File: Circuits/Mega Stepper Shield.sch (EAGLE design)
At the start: 14 parts

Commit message: Update CAD
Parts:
- removed POWER, STBY, STOP-1, STOP-2, STOP-3: (no value), con-wago-500:W237-102
- added EXTERNAL: (no value), con-wago-508:W237-09P
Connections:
- net 12V10A: now also EXTERNAL-1.KL; no longer POWER-1.KL
- net GND: now also EXTERNAL-3.KL, EXTERNAL-6.KL; no longer STBY-1.KL, STOP-1-2.KL, STOP-2-2.KL, STOP-3-2.KL
- net N$1: now also EXTERNAL-9.KL; no longer STOP-3-1.KL
- net N$11: now also EXTERNAL-2.KL; no longer POWER-2.KL
- net N$12: now also EXTERNAL-8.KL; no longer STOP-2-1.KL
- net N$13: now also EXTERNAL-4.KL; no longer STBY-2.KL
- net N$14: now also EXTERNAL-7.KL; no longer STOP-1-1.KL
- net N$2: now also EXTERNAL-5.KL

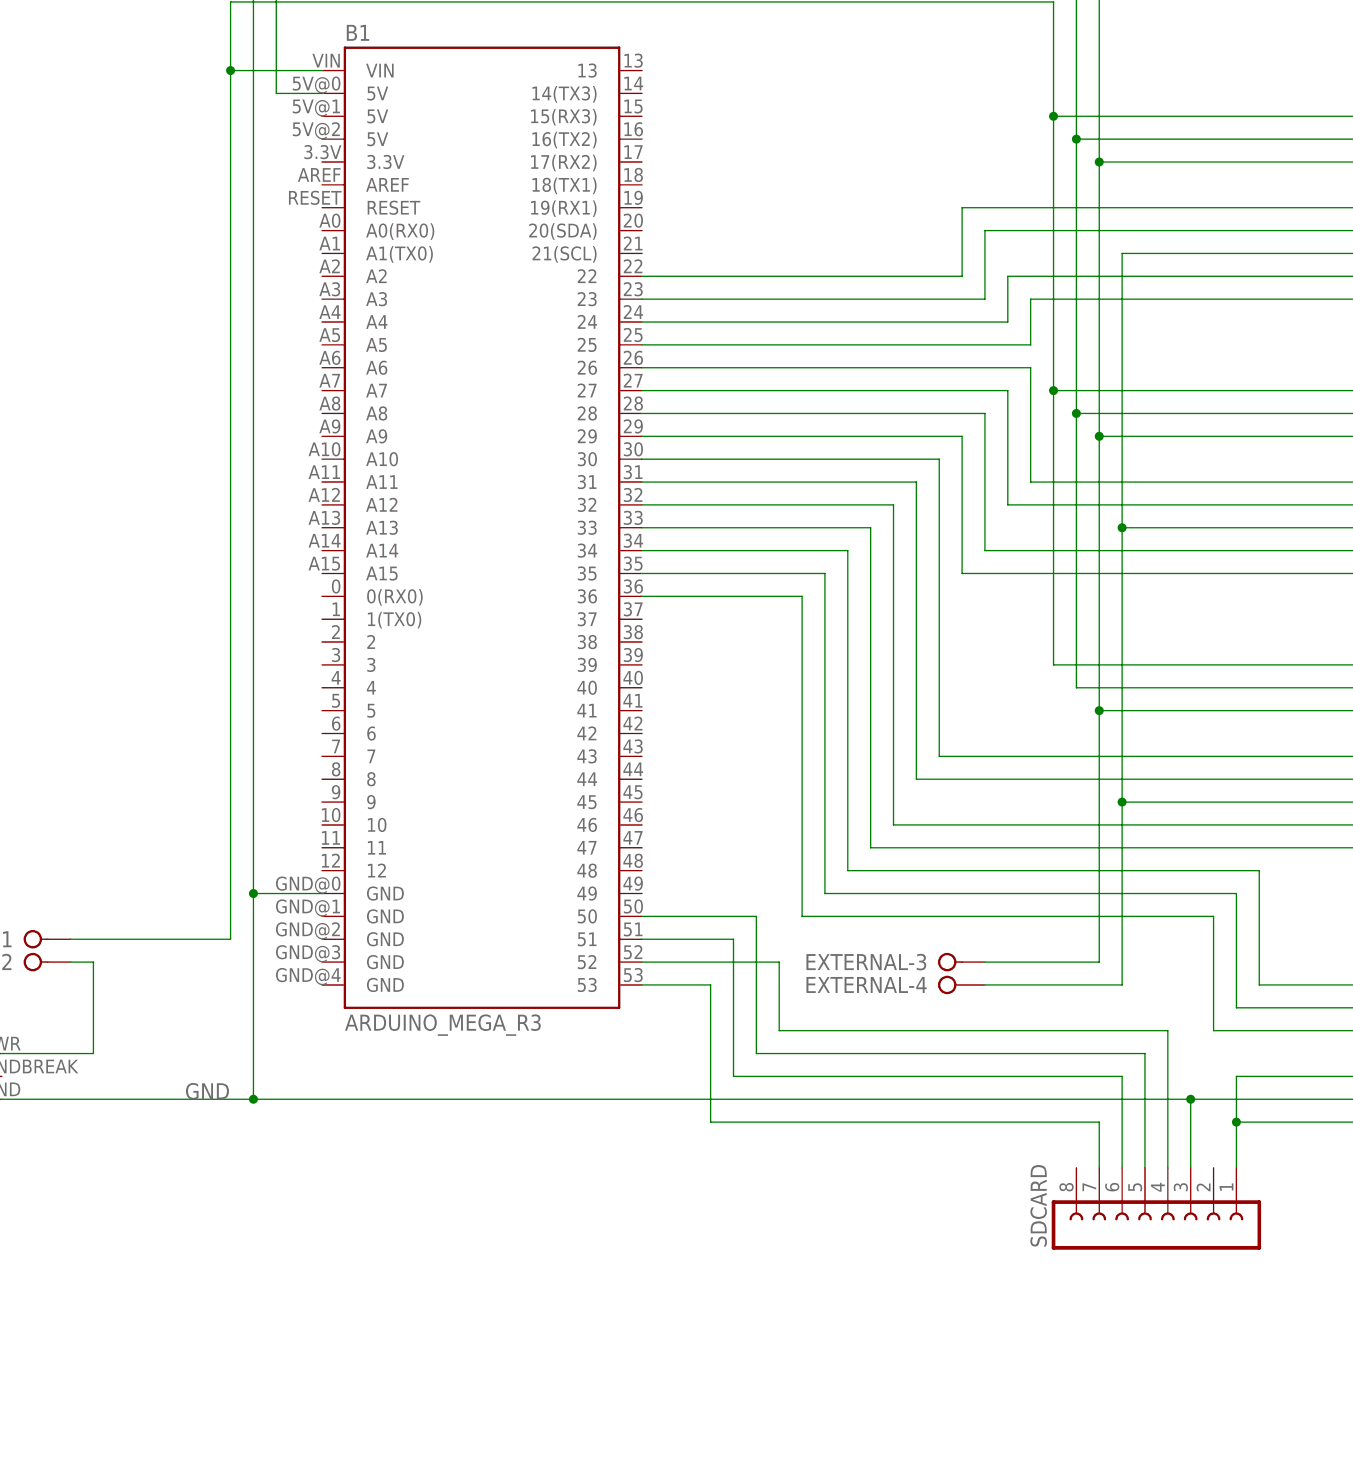
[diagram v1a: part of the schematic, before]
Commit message: Update schematic and prototype schematic
Added RF module to schematic, created a prototype sub board for multiple stepper control
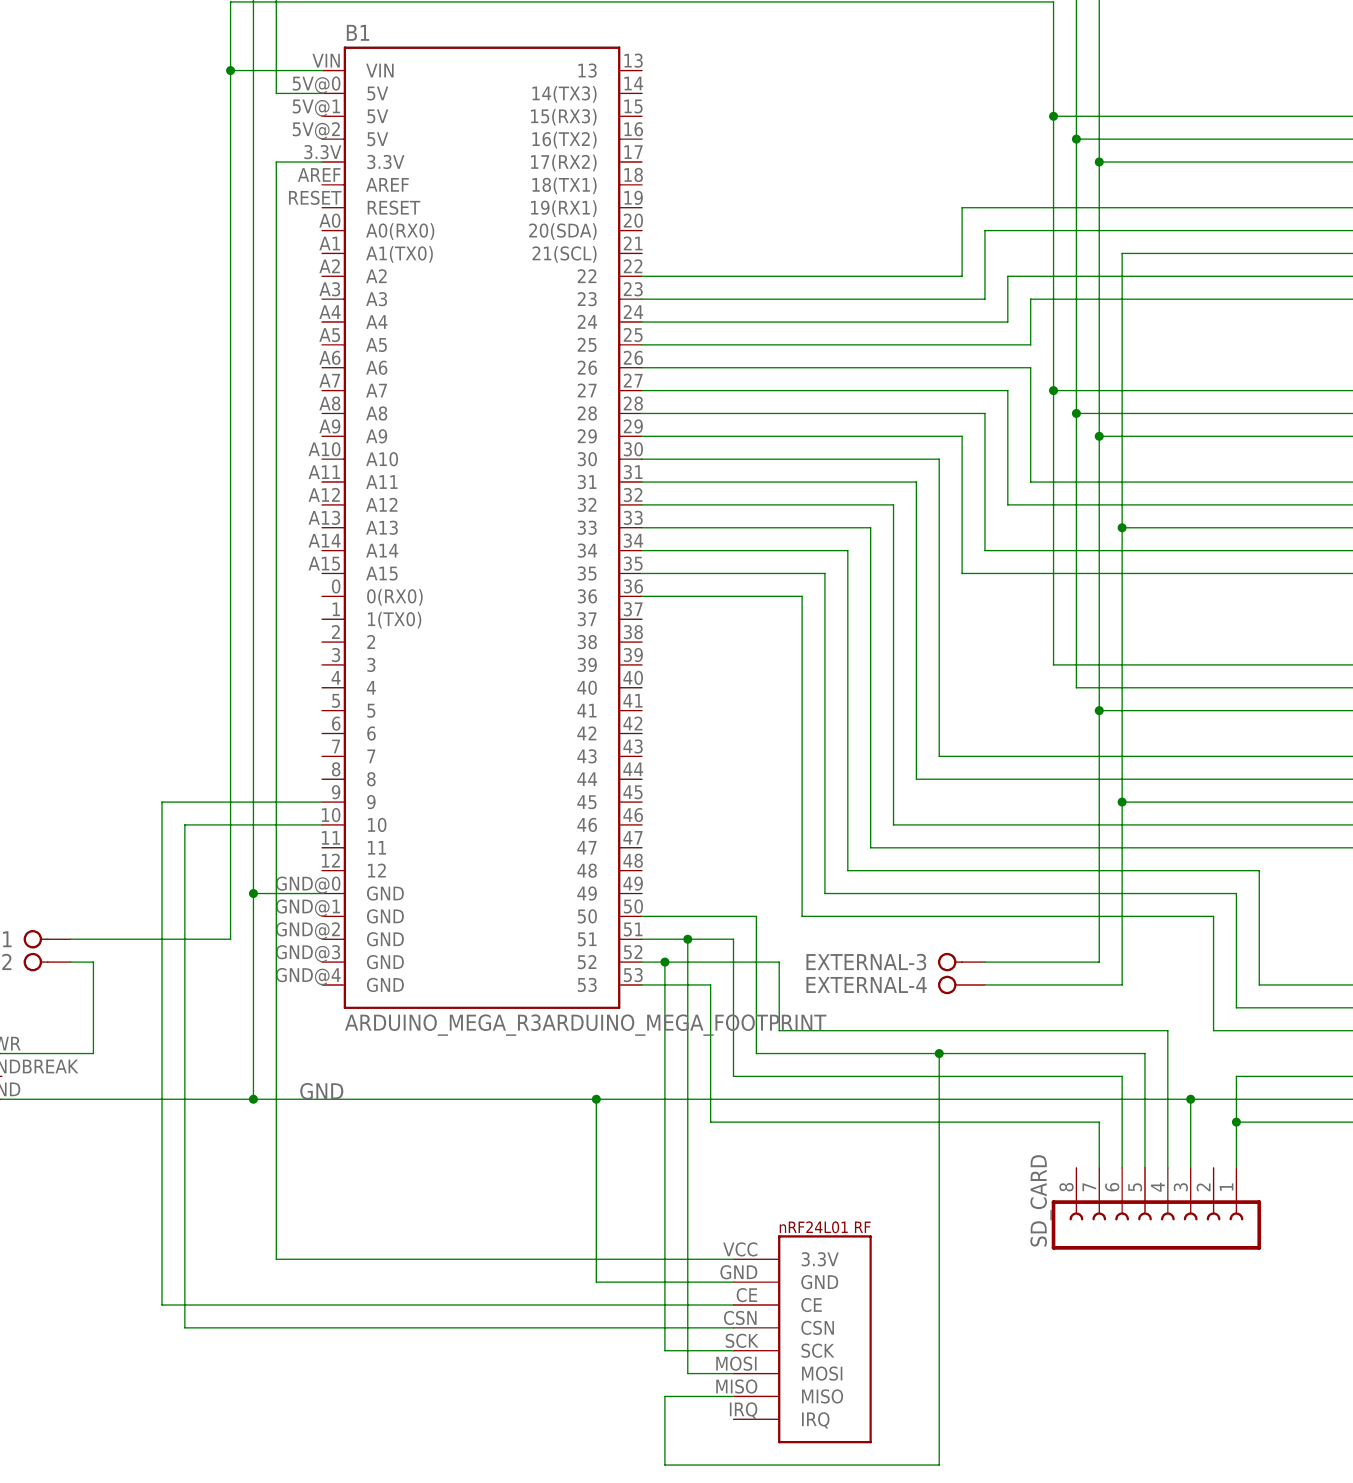
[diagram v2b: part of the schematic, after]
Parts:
- added U$1: NRF24L01_RF_MODULE, SparkFun-Boards-Expanded:NRF24L01_RF_MODULE
- B1: value ARDUINO_MEGA_R3 -> ARDUINO_MEGA_R3ARDUINO_MEGA_FOOTPRINT; device SparkFun-Boards-Expanded:ARDUINO_MEGA_R3 -> SparkFun-Boards-Expanded:ARDUINO_MEGA_R3ARDUINO_MEGA_FOOTPRINT
- renumbered SDCARD to SD_CARD
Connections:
- new net N$32: B1.3.3V, U$1.3.3V
- new net N$34: B1.9, U$1.CE
- new net N$35: B1.10, U$1.CSN
- net GND: now also U$1.GND
- net N$28: now also U$1.SCK
- net N$29: now also U$1.MISO
- net N$30: now also U$1.MOSI
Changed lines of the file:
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@@
 </classes>
 <parts>
-<part name="B1" library="SparkFun-Boards-Expanded" deviceset="ARDUINO_MEGA_R3" device=""/>
+<part name="B1" library="SparkFun-Boards-Expanded" deviceset="ARDUINO_MEGA_R3" device="ARDUINO_MEGA_FOOTPRINT" value="ARDUINO_MEGA_R3ARDUINO_MEGA_FOOTPRINT"/>
 <part name="STEPPER-1-CON" library="SparkFun-Boards-Expanded" deviceset="TB6612-BREAKOUT-MOTOR-CONTROLLER" device=""/>
 <part name="STEPPER-2-CON" library="SparkFun-Boards-Expanded" deviceset="TB6612-BREAKOUT-MOTOR-CONTROLLER" device=""/>
@@
 <part name="STEPPER-3" library="pinhead" library_urn="urn:adsk.eagle:library:325" deviceset="PINHD-1X4" device="" package3d_urn="urn:adsk.eagle:package:22407/2"/>
 <part name="CN1" library="adafruit" library_urn="urn:adsk.eagle:library:420" deviceset="DCBARREL" device="PTH" package3d_urn="urn:adsk.eagle:package:6240729/1"/>
-<part name="SDCARD" library="con-lsta" library_urn="urn:adsk.eagle:library:161" deviceset="FE08-1" device="" package3d_urn="urn:adsk.eagle:package:8194/1"/>
+<part name="SD_CARD" library="con-lsta" library_urn="urn:adsk.eagle:library:161" deviceset="FE08-1" device="" package3d_urn="urn:adsk.eagle:package:8194/1"/>
 <part name="EXTERNAL" library="con-wago-508" library_urn="urn:adsk.eagle:library:196" deviceset="W237-09P" device="" package3d_urn="urn:adsk.eagle:package:10748/1"/>
+<part name="U$1" library="SparkFun-Boards-Expanded" deviceset="NRF24L01_RF_MODULE" device=""/>
 </parts>
 <sheets>
@@
 <attribute name="VALUE" x="-76.2" y="-66.04" size="1.27" layer="96"/>
 </instance>
-<instance part="SDCARD" gate="G$1" x="60.96" y="-78.74" smashed="yes" rot="R90">
+<instance part="SD_CARD" gate="G$1" x="60.96" y="-78.74" smashed="yes" rot="R90">
 <attribute name="VALUE" x="73.66" y="-80.01" size="1.778" layer="96" rot="R90"/>
 <attribute name="NAME" x="47.498" y="-80.01" size="1.778" layer="95" rot="R90"/>
@@
 <attribute name="NAME" x="135.89" y="-34.671" size="1.778" layer="95" rot="R180"/>
 </instance>
+<instance part="U$1" gate="G$1" x="25.4" y="-81.28" smashed="yes"/>
 </instances>
 <busses>
@@
 <junction x="86.36" y="38.1"/>
 <junction x="86.36" y="-38.1"/>
-<pinref part="SDCARD" gate="G$1" pin="1"/>
+<pinref part="SD_CARD" gate="G$1" pin="1"/>
 <wire x1="68.58" y1="-71.12" x2="68.58" y2="-66.04" width="0.1524" layer="91"/>
 <wire x1="68.58" y1="-66.04" x2="68.58" y2="-60.96" width="0.1524" layer="91"/>
@@
 <wire x1="-40.64" y1="-63.5" x2="-40.64" y2="-40.64" width="0.1524" layer="91"/>
 <junction x="-40.64" y="-40.64"/>
-<label x="-48.26" y="-63.5" size="1.778" layer="95"/>
-<wire x1="-40.64" y1="-63.5" x2="63.5" y2="-63.5" width="0.1524" layer="91"/>
+<label x="-35.56" y="-63.5" size="1.778" layer="95"/>
 <junction x="-40.64" y="-63.5"/>
-<pinref part="SDCARD" gate="G$1" pin="3"/>
+<pinref part="SD_CARD" gate="G$1" pin="3"/>
+<wire x1="-40.64" y1="-63.5" x2="-2.54" y2="-63.5" width="0.1524" layer="91"/>
+<wire x1="-2.54" y1="-63.5" x2="63.5" y2="-63.5" width="0.1524" layer="91"/>
 <wire x1="63.5" y1="-71.12" x2="63.5" y2="-63.5" width="0.1524" layer="91"/>
 <pinref part="EXTERNAL" gate="-6" pin="KL"/>
@@
 <pinref part="EXTERNAL" gate="-3" pin="KL"/>
 <wire x1="40.64" y1="-48.26" x2="53.34" y2="-48.26" width="0.1524" layer="91"/>
+<pinref part="U$1" gate="G$1" pin="GND"/>
+<wire x1="12.7" y1="-83.82" x2="-2.54" y2="-83.82" width="0.1524" layer="91"/>
+<wire x1="-2.54" y1="-83.82" x2="-2.54" y2="-63.5" width="0.1524" layer="91"/>
+<junction x="-2.54" y="-63.5"/>
 </segment>
 </net>
@@
 <net name="N$28" class="0">
 <segment>
-<pinref part="SDCARD" gate="G$1" pin="4"/>
+<pinref part="SD_CARD" gate="G$1" pin="4"/>
 <wire x1="60.96" y1="-71.12" x2="60.96" y2="-55.88" width="0.1524" layer="91"/>
 <wire x1="60.96" y1="-55.88" x2="17.78" y2="-55.88" width="0.1524" layer="91"/>
 <pinref part="B1" gate="G$1" pin="52"/>
 <wire x1="17.78" y1="-55.88" x2="17.78" y2="-48.26" width="0.1524" layer="91"/>
-<wire x1="17.78" y1="-48.26" x2="2.54" y2="-48.26" width="0.1524" layer="91"/>
+<wire x1="17.78" y1="-48.26" x2="5.08" y2="-48.26" width="0.1524" layer="91"/>
+<pinref part="U$1" gate="G$1" pin="SCK"/>
+<wire x1="5.08" y1="-48.26" x2="2.54" y2="-48.26" width="0.1524" layer="91"/>
+<wire x1="5.08" y1="-48.26" x2="5.08" y2="-91.44" width="0.1524" layer="91"/>
+<wire x1="5.08" y1="-91.44" x2="12.7" y2="-91.44" width="0.1524" layer="91"/>
+<junction x="5.08" y="-48.26"/>
 </segment>
 </net>
@@
 <wire x1="2.54" y1="-43.18" x2="15.24" y2="-43.18" width="0.1524" layer="91"/>
 <wire x1="15.24" y1="-43.18" x2="15.24" y2="-58.42" width="0.1524" layer="91"/>
-<pinref part="SDCARD" gate="G$1" pin="5"/>
-<wire x1="15.24" y1="-58.42" x2="58.42" y2="-58.42" width="0.1524" layer="91"/>
+<pinref part="SD_CARD" gate="G$1" pin="5"/>
+<wire x1="15.24" y1="-58.42" x2="35.56" y2="-58.42" width="0.1524" layer="91"/>
+<wire x1="35.56" y1="-58.42" x2="58.42" y2="-58.42" width="0.1524" layer="91"/>
 <wire x1="58.42" y1="-58.42" x2="58.42" y2="-71.12" width="0.1524" layer="91"/>
+<pinref part="U$1" gate="G$1" pin="MISO"/>
+<wire x1="12.7" y1="-96.52" x2="5.08" y2="-96.52" width="0.1524" layer="91"/>
+<wire x1="5.08" y1="-96.52" x2="5.08" y2="-104.14" width="0.1524" layer="91"/>
+<wire x1="5.08" y1="-104.14" x2="35.56" y2="-104.14" width="0.1524" layer="91"/>
+<wire x1="35.56" y1="-104.14" x2="35.56" y2="-58.42" width="0.1524" layer="91"/>
+<junction x="35.56" y="-58.42"/>
 </segment>
 </net>
 <net name="N$30" class="0">
 <segment>
-<pinref part="SDCARD" gate="G$1" pin="6"/>
+<pinref part="SD_CARD" gate="G$1" pin="6"/>
 <wire x1="55.88" y1="-71.12" x2="55.88" y2="-60.96" width="0.1524" layer="91"/>
 <wire x1="55.88" y1="-60.96" x2="12.7" y2="-60.96" width="0.1524" layer="91"/>
 <pinref part="B1" gate="G$1" pin="51"/>
 <wire x1="12.7" y1="-60.96" x2="12.7" y2="-45.72" width="0.1524" layer="91"/>
-<wire x1="12.7" y1="-45.72" x2="2.54" y2="-45.72" width="0.1524" layer="91"/>
+<wire x1="12.7" y1="-45.72" x2="7.62" y2="-45.72" width="0.1524" layer="91"/>
+<pinref part="U$1" gate="G$1" pin="MOSI"/>
+<wire x1="7.62" y1="-45.72" x2="2.54" y2="-45.72" width="0.1524" layer="91"/>
+<wire x1="12.7" y1="-93.98" x2="7.62" y2="-93.98" width="0.1524" layer="91"/>
+<wire x1="7.62" y1="-93.98" x2="7.62" y2="-45.72" width="0.1524" layer="91"/>
+<junction x="7.62" y="-45.72"/>
 </segment>
 </net>
@@
 <wire x1="2.54" y1="-50.8" x2="10.16" y2="-50.8" width="0.1524" layer="91"/>
 <wire x1="10.16" y1="-50.8" x2="10.16" y2="-66.04" width="0.1524" layer="91"/>
-<pinref part="SDCARD" gate="G$1" pin="7"/>
+<pinref part="SD_CARD" gate="G$1" pin="7"/>
 <wire x1="10.16" y1="-66.04" x2="53.34" y2="-66.04" width="0.1524" layer="91"/>
 <wire x1="53.34" y1="-66.04" x2="53.34" y2="-71.12" width="0.1524" layer="91"/>
 </segment>
 </net>
+<net name="N$32" class="0">
+<segment>
+<pinref part="B1" gate="G$1" pin="3.3V"/>
+<wire x1="-33.02" y1="40.64" x2="-38.1" y2="40.64" width="0.1524" layer="91"/>
+<wire x1="-38.1" y1="40.64" x2="-38.1" y2="-81.28" width="0.1524" layer="91"/>
+<pinref part="U$1" gate="G$1" pin="3.3V"/>
+<wire x1="-38.1" y1="-81.28" x2="12.7" y2="-81.28" width="0.1524" layer="91"/>
+</segment>
+</net>
+<net name="N$34" class="0">
+<segment>
+<pinref part="B1" gate="G$1" pin="9"/>
+<wire x1="-33.02" y1="-30.48" x2="-50.8" y2="-30.48" width="0.1524" layer="91"/>
+<wire x1="-50.8" y1="-30.48" x2="-50.8" y2="-86.36" width="0.1524" layer="91"/>
+<pinref part="U$1" gate="G$1" pin="CE"/>
+<wire x1="-50.8" y1="-86.36" x2="12.7" y2="-86.36" width="0.1524" layer="91"/>
+</segment>
+</net>
+<net name="N$35" class="0">
+<segment>
+<pinref part="U$1" gate="G$1" pin="CSN"/>
+<wire x1="12.7" y1="-88.9" x2="-48.26" y2="-88.9" width="0.1524" layer="91"/>
+<wire x1="-48.26" y1="-88.9" x2="-48.26" y2="-33.02" width="0.1524" layer="91"/>
+<pinref part="B1" gate="G$1" pin="10"/>
+<wire x1="-48.26" y1="-33.02" x2="-33.02" y2="-33.02" width="0.1524" layer="91"/>
+</segment>
+</net>

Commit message: Update Board Design
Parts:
- removed EXTERNAL: (no value), con-wago-508:W237-09P
- added ENDSTOP: (no value), con-wago-508:W237-05P
- added ERROR: YELLOW, adafruit:LED5MM
- added ESTOP: (no value), con-wago-508:W237-3E
- added E_STOP: RED, adafruit:LED5MM
- added MAGNET, POWER: (no value), con-wago-508:W237-02P
- added NOMINAL: GREEN, adafruit:LED5MM
- added R1, R2, R3: 220 Ohm, adafruit:R-US_0204/7
- added T1: 2N2222, adafruit:2N2222
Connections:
- net N$32 renamed 3.3V
- removed net N$2: B1.5V@0, EXTERNAL-5.KL, SD_CARD.1, STEPPER-1-CON.PWMA, STEPPER-1-CON.PWMB, STEPPER-1-CON.VCC, STEPPER-2-CON.PWMA, STEPPER-2-CON.PWMB, STEPPER-2-CON.VCC, STEPPER-3-CON.PWMA, STEPPER-3-CON.PWMB, STEPPER-3-CON.VCC
- new net 5V: B1.5V@0, ENDSTOP-4.KL, ESTOP-1.KL, SD_CARD.1, STEPPER-1-CON.PWMA, STEPPER-1-CON.PWMB, STEPPER-1-CON.VCC, STEPPER-2-CON.PWMA, STEPPER-2-CON.PWMB, STEPPER-2-CON.VCC, STEPPER-3-CON.PWMA, STEPPER-3-CON.PWMB, STEPPER-3-CON.VCC
- new net N$33: NOMINAL.A, R3.2
- new net N$36: ERROR.A, R2.2
- new net N$37: E_STOP.A, R1.2
- new net N$38: B1.38, R1.1
- new net N$39: B1.39, R2.1
- new net N$40: B1.40, R3.1
- new net N$41: B1.2, T1.B
- new net N$42: MAGNET-1.KL, T1.E
- net 12V10A: now also POWER-1.KL, T1.C; no longer EXTERNAL-1.KL
- net GND: now also ENDSTOP-5.KL, ERROR.C, ESTOP-3.KL, E_STOP.C, MAGNET-2.KL, NOMINAL.C; no longer EXTERNAL-3.KL, EXTERNAL-6.KL
- net N$1: now also ENDSTOP-3.KL; no longer EXTERNAL-9.KL
- net N$11: now also POWER-2.KL; no longer EXTERNAL-2.KL
- net N$12: now also ENDSTOP-2.KL; no longer EXTERNAL-8.KL
- net N$13: now also B1.37, ESTOP-2.KL; no longer EXTERNAL-4.KL
- net N$14: now also ENDSTOP-1.KL; no longer EXTERNAL-7.KL
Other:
- moved on the sheet: SD_CARD, STEPPER-1, STEPPER-1-CON, STEPPER-2, STEPPER-2-CON, STEPPER-3, STEPPER-3-CON
